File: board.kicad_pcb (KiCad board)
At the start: 4 copper layers, 55 x 52 mm, 62 parts, among them J1 PROVISIONAL_PS1_BARE_MALE_PIN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, J2 USB-C USB2 HRO TYPE-C-31-M-12, Q1 2N7002 DATA OD, Q2 2N7002 ACK OD, Q3 MMBT3904 AUTO-BOOT, Q4 MMBT3904 AUTO-RESET, SW1 RESET, SW2 BOOT, U1 ESP32-WROOM-32, U2 AP63203WU-7 3.3V 2A PS1 BUCK, U3 AP2112K-3.3 USB LDO, U4 TPS2113APW POWER MUX, U5 CH340C USB-UART, U6 USBLC6-2SC6 ESD

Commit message: Archive 55x52 WIP board checkpoint
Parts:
- D3, D4, D5: footprint PlayBridge:D_SOD-323 -> PlayBridge:D_SOD-323_SILK_CLEAN
- J1: footprint PlayBridge:PROVISIONAL_PS1_MALE_PIN_ARRAY_P4.00_SQ0.64_MECH_TBD_3D_DIAGNOSTIC -> PlayBridge:PROVISIONAL_PS1_MALE_PIN_ARRAY_P4.00_SQ0.64_P16.00_MECH_TBD_3D
- J2: footprint PlayBridge:USB_C_Receptacle_HRO_TYPE-C-31-M-12_FANOUT -> PlayBridge:USB_C_Receptacle_HRO_TYPE-C-31-M-12_INTERIOR_FANOUT_V14_C165948_MODEL
- Q1, Q2, Q3, Q4: footprint PlayBridge:SOT-23 -> PlayBridge:SOT-23_SILK_CLEAN_V2
- R1, R10, R11, R12, R13, R16, R17, R18, R19, R2, R20, R3, R4, R5, R6, R7, R8, R9: footprint PlayBridge:R_0603_1608Metric -> PlayBridge:R_0603_1608Metric_SILK_CLEAN
- R14, R15, R21, R22, R23, R24: footprint PlayBridge:R_0402_1005Metric -> PlayBridge:R_0402_1005Metric_SILK_CLEAN
- SW1: footprint PlayBridge:SW_SPST_CK_RS282G05A3 -> PlayBridge:SW_SPST_CK_RS282G05A3_RESET_SILK_V7
- SW2: footprint PlayBridge:SW_SPST_CK_RS282G05A3 -> PlayBridge:SW_SPST_CK_RS282G05A3_BOOT_SILK_V7
- TP1, TP2, TP3, TP4: footprint PlayBridge:TestPoint_Pad_D1.5mm -> PlayBridge:TestPoint_Pad_D1.5mm_SILK_CLEAN
- U1: footprint PlayBridge:ESP32-WROOM-32_D0.3mm -> PlayBridge:ESP32-WROOM-32_D0.3mm_SILK_CLEAN
- U5: footprint PlayBridge:SOIC-16_3.9x9.9mm_P1.27mm -> PlayBridge:SOIC-16_3.9x9.9mm_P1.27mm_SILK_CLEAN
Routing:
- net GND: track 305.9 -> 0.00 mm, vias 9 -> 0
- net 3V3: track 131.8 -> 0.00 mm, vias 5 -> 0
- net EN: track 60.9 -> 0.00 mm, vias 5 -> 0
- net PS_3V3: track 50.0 -> 0.00 mm, vias 3 -> 0
- net USB_5V: track 49.6 -> 0.00 mm, vias 6 -> 0
- net BOOT: track 41.8 -> 0.00 mm, vias 3 -> 0
- net PS_CMD: track 39.5 -> 0.00 mm, vias 1 -> 0
- net DATA_GATE: track 39.2 -> 0.00 mm, vias 2 -> 0
- net PS_DATA: track 37.6 -> 0.00 mm, vias 1 -> 0
- net ATT_IN: track 37.4 -> 0.00 mm, vias 3 -> 0
- net ACK_GATE: track 36.5 -> 0.00 mm, vias 2 -> 0
- net UART_TX: track 34.9 -> 0.00 mm, vias 3 -> 0
- net CLK_IN: track 30.2 -> 0.00 mm, vias 2 -> 0
- net CMD_IN: track 29.4 -> 0.00 mm, vias 2 -> 0
- net STATUS_LED: track 28.3 -> 0.00 mm, vias 2 -> 0
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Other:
- board size 55 x 52 mm -> 50 x 52 mm

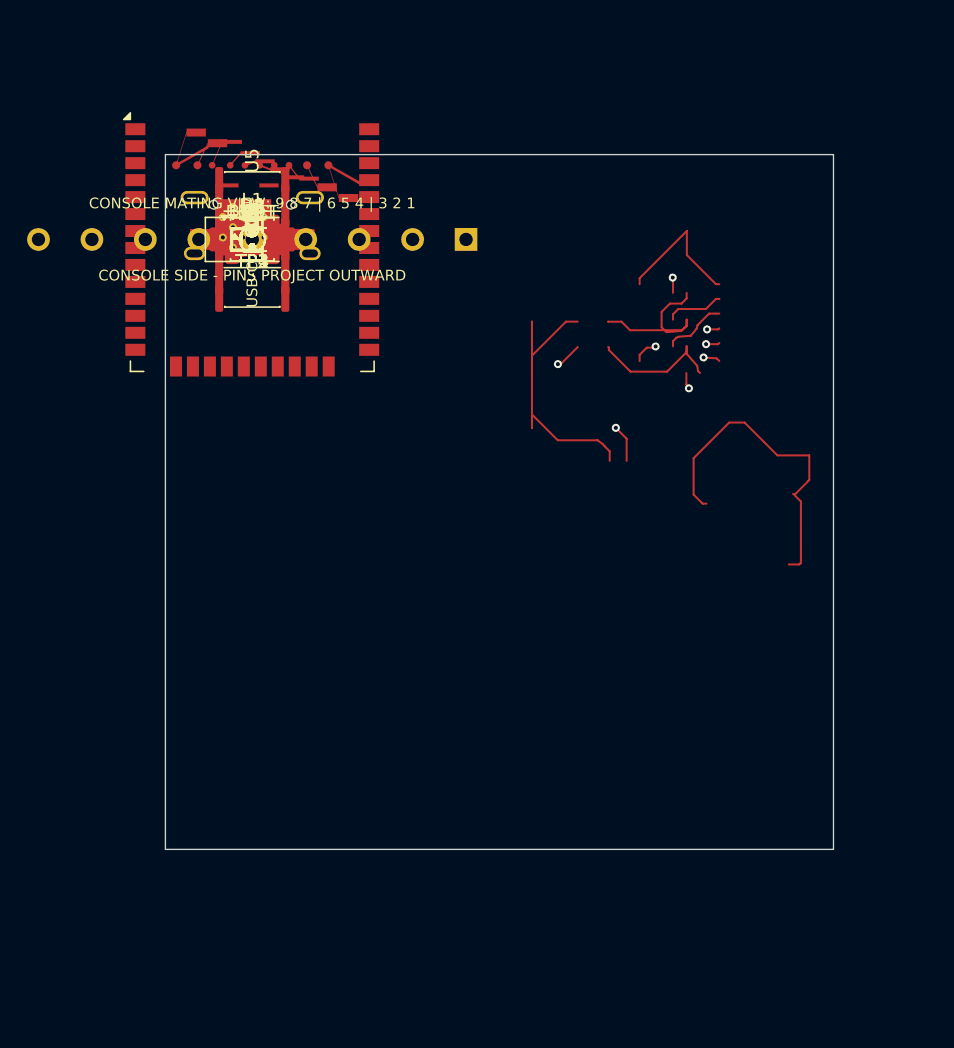
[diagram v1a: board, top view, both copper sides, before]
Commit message: Checkpoint routed 55x52 PlayBridge board and reviewed renders
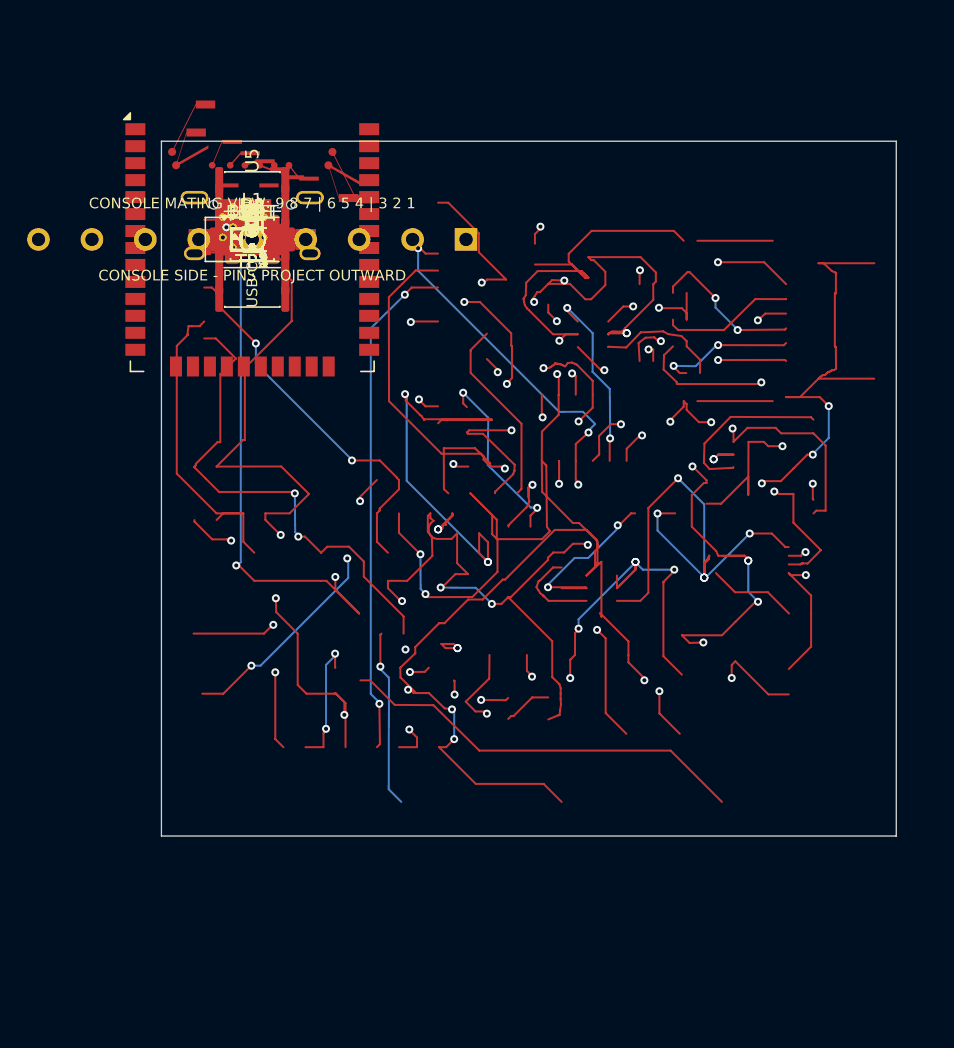
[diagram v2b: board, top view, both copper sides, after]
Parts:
- added R25: 0R USB LDO ENABLE, PlayBridge:R_0402_1005Metric_SILK_CLEAN, F.Cu at (0.00, 0.00)
- added R26: 0R USB VBUS A JOIN, PlayBridge:R_0402_1005Metric_SILK_CLEAN, F.Cu at (0.00, 0.00)
- added R27: 0R USB VBUS B JOIN, PlayBridge:R_0402_1005Metric_SILK_CLEAN, F.Cu at (0.00, 0.00)
- added R28: 0R USB UART SUPPLY JOIN, PlayBridge:R_0402_1005Metric_SILK_CLEAN, F.Cu at (0.00, 0.00)
- J2: footprint PlayBridge:USB_C_Receptacle_HRO_TYPE-C-31-M-12_INTERIOR_FANOUT_V14_C165948_MODEL -> PlayBridge:USB_C_Receptacle_HRO_TYPE-C-31-M-12_INTERIOR_FANOUT_V16_C165948_MODEL
- SW1: value RESET -> RESET K2-1107ST-A4SW-06; footprint PlayBridge:SW_SPST_CK_RS282G05A3_RESET_SILK_V7 -> PlayBridge:SW_SPST_HRO_K2-1107ST-A4SW-06_RESET_V8
- SW2: value BOOT -> BOOT K2-1107ST-A4SW-06; footprint PlayBridge:SW_SPST_CK_RS282G05A3_BOOT_SILK_V7 -> PlayBridge:SW_SPST_HRO_K2-1107ST-A4SW-06_BOOT_V8
- U4: footprint PlayBridge:TSSOP-8_3x3mm_P0.65mm -> PlayBridge:TSSOP-8_3x3mm_P0.65mm_U4_ESCAPE_V2
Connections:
- J2 pad A4_B9: USB_5V -> USB_VBUS_A
- J2 pad A9_B4: USB_5V -> USB_VBUS_B
- U3 pad 3: USB_5V -> USB_LDO_EN
- U5 pad 16: USB_5V -> USB_UART_5V
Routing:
- net GND: track 0.00 -> 320.8 mm, vias 0 -> 28
- net 3V3: track 0.00 -> 110.4 mm, vias 0 -> 8
- net EN: track 0.00 -> 79.8 mm, vias 0 -> 9
- net USB_5V: track 0.00 -> 62.4 mm, vias 0 -> 4
- net BOOT: track 0.00 -> 58.5 mm, vias 0 -> 5
- net PS_3V3: track 0.00 -> 57.9 mm, vias 0 -> 8
- net UART_RX: track 0.00 -> 56.3 mm, vias 0 -> 2
- net UART_TX: track 0.00 -> 46.8 mm, vias 0 -> 4
- net PS_CMD: track 0.00 -> 44.2 mm, vias 0 -> 1
- net DATA_GATE: track 0.00 -> 38.3 mm, vias 0 -> 2
- net ACK_GATE: track 0.00 -> 38.0 mm, vias 0 -> 2
- net CLK_IN: track 0.00 -> 36.9 mm, vias 0 -> 2
- net PS_8V: track 0.00 -> 33.4 mm, vias 0 -> 6
- net PS_DATA: track 0.00 -> 30.8 mm
- net ATT_IN: track 0.00 -> 28.7 mm, vias 0 -> 2
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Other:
- board size 50 x 52 mm -> 55 x 52 mm

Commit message: Add V2 modular donor harness board checkpoint
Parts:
- added J3: USB-C USB2 HRO TYPE-C-31-M-12 PROGRAMMING, PlayBridge:USB_C_Receptacle_HRO_TYPE-C-31-M-12_INTERIOR_FANOUT_V16_C165948_MODEL, F.Cu at (0.00, 0.00)
- J1: value PROVISIONAL_PS1_BARE_MALE_PIN_ARRAY MECHANICAL_TBD NOT_FOR_PRODUCTION -> PS1 DONOR HARNESS / NOT USB; footprint PlayBridge:PROVISIONAL_PS1_MALE_PIN_ARRAY_P4.00_SQ0.64_P16.00_MECH_TBD_3D -> PlayBridge:USB3_A_Molex_48393-0003_AUTHORIZED_COPY
- J2: value USB-C USB2 HRO TYPE-C-31-M-12 -> RESERVED REAR SERIAL / NOT USB / ALL CONTACTS NC; footprint PlayBridge:USB_C_Receptacle_HRO_TYPE-C-31-M-12_INTERIOR_FANOUT_V16_C165948_MODEL -> PlayBridge:USB3_A_Molex_48393-0003_RESERVED_NOT_USB_V2
- U4: footprint PlayBridge:TSSOP-8_3x3mm_P0.65mm_U4_ESCAPE_V2 -> PlayBridge:TSSOP-8_3x3mm_P0.65mm_AUTHORIZED_KICAD_COPY
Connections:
- D3 pad 1: 3V3 -> PS_3V3
- D4 pad 1: 3V3 -> PS_3V3
- D5 pad 1: 3V3 -> PS_3V3
- J1 pad 1: PS_DATA -> (no net)
- J1 pad 3: PS_8V_RAW -> PS_CLK
- J1 pad 5: (no net) -> PS_ATT
- J1 pad 6: PS_ATT -> PS_DATA
- J1 pad 7: PS_CLK -> PS_ACK
- J1 pad 8: (no net) -> PS_8V_RAW
- J1 pad 9: PS_ACK -> (no net)
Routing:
- net GND: track 320.8 -> 0.00 mm, vias 28 -> 0
- net 3V3: track 110.4 -> 0.00 mm, vias 8 -> 0
- net USB_5V: track 62.4 -> 0.00 mm, vias 4 -> 0
- net PS_3V3: track 57.9 -> 0.00 mm, vias 8 -> 0
- net UART_RX: track 56.3 -> 88.4 mm, vias 2 -> 8
- net PS_CLK: track 13.4 -> 41.6 mm, vias 1 -> 3
- net USB_3V3: track 25.3 -> 0.00 mm, vias 2 -> 0
- net AUTO_RESET: track 14.2 -> 34.4 mm, vias 0 -> 4
- net PS_ACK: track 18.0 -> 37.6 mm, vias 1 -> 3
- net PS_8V_RAW: track 18.6 -> 0.00 mm, vias 1 -> 0
- net USB_DTR: track 23.0 -> 40.7 mm
- net USB_DP_B: track 9.98 -> 27.0 mm, vias 0 -> 4
- net PS_DATA: track 30.8 -> 14.4 mm, vias 0 -> 1
- net PS_8V: track 33.4 -> 18.3 mm, vias 6 -> 2
- net USB_DP: track 14.1 -> 0.00 mm, vias 2 -> 0
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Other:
- board size 55 x 52 mm -> 55 x 62 mm
- copper layers 4 -> 2

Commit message: Align V2 USB-A footprints with Molex mechanics
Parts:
- J1: footprint PlayBridge:USB3_A_Molex_48393-0003_AUTHORIZED_COPY -> PlayBridge:USB3_A_Molex_48393-0003_AUTHORIZED_COPY_MODEL_V3
- J2: footprint PlayBridge:USB3_A_Molex_48393-0003_RESERVED_NOT_USB_V2 -> PlayBridge:USB3_A_Molex_48393-0003_RESERVED_NOT_USB_MODEL_V3
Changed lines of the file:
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@@
 	(generator_version "10.99")
 	(general
-		(thickness 1.6)
+		(thickness 1.2)
 		(legacy_teardrops no)
 	)
@@
 		)
 	)
-	(footprint "PlayBridge:USB3_A_Molex_48393-0003_AUTHORIZED_COPY"
+	(footprint "PlayBridge:USB3_A_Molex_48393-0003_AUTHORIZED_COPY_MODEL_V3"
 		(placed yes)
 		(layer "F.Cu")
@@
 			(remove_unused_layers no)
 		)
+		(model "${KIPRJMOD}/PlayBridge.3dshapes/Molex_48393-0003_TraceParts_exact_visual.wrl"
+			(offset (xyz 3.5 -2.5 1.732204724))
+			(scale (xyz 0.3937007874 0.3937007874 0.3937007874))
+			(rotate (xyz -90 0 0))
+		)
 		(embedded_fonts no)
 	)
@@
 		)
 	)
-	(footprint "PlayBridge:USB3_A_Molex_48393-0003_RESERVED_NOT_USB_V2"
+	(footprint "PlayBridge:USB3_A_Molex_48393-0003_RESERVED_NOT_USB_MODEL_V3"
 		(layer "F.Cu")
 		(transform
@@
 			(remove_unused_layers no)
 		)
+		(model "${KIPRJMOD}/PlayBridge.3dshapes/Molex_48393-0003_TraceParts_exact_visual.wrl"
+			(offset (xyz 3.5 -2.5 1.732204724))
+			(scale (xyz 0.3937007874 0.3937007874 0.3937007874))
+			(rotate (xyz -90 0 0))
+		)
 		(embedded_fonts no)
